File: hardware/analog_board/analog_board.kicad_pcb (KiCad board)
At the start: 4 copper layers, 125 x 90 mm, 295 parts, among them J1 2x5 牛角座, J2 Conn_02x08_Counter_Clockwise, J3 Conn_01x04_Pin, J4 Conn_01x08, J5 CH1, J6 CH1, J7 CH1, Q1 MMBT3906, Q2 MMBT3906, U1 GW2A-LV18EQ144, U11 TPS62933, U12 L7805, U13 L7905, U14 TPS7A4701xRGW, U15 TPS7A91, U19 AMS1117, U2 GD25Q32JVSS, U3 AD9747BCPZ, U4 OPA695ID, U5 OPA695ID, U6 NE5532, U8 CDCI6214RGER, Y1 ASE-10MHz

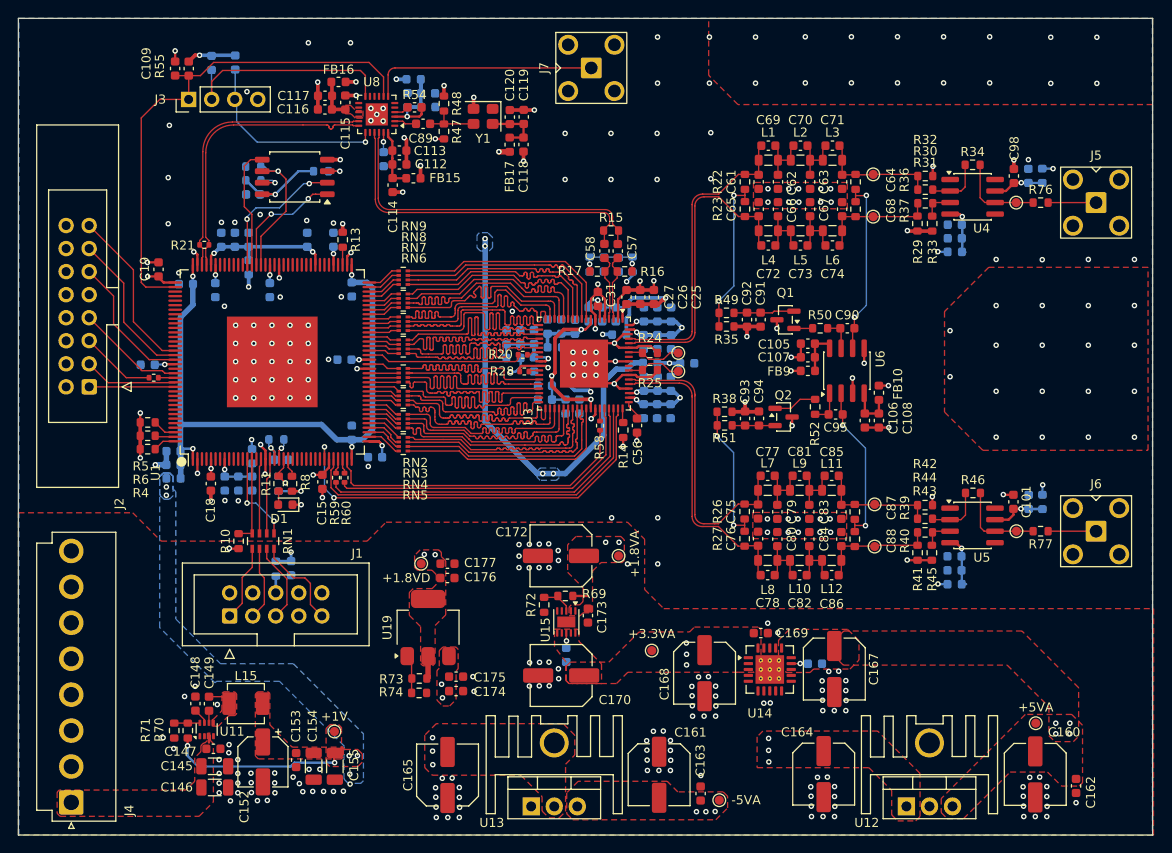
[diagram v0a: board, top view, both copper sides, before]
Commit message: debug：修正 PCB 部分错误
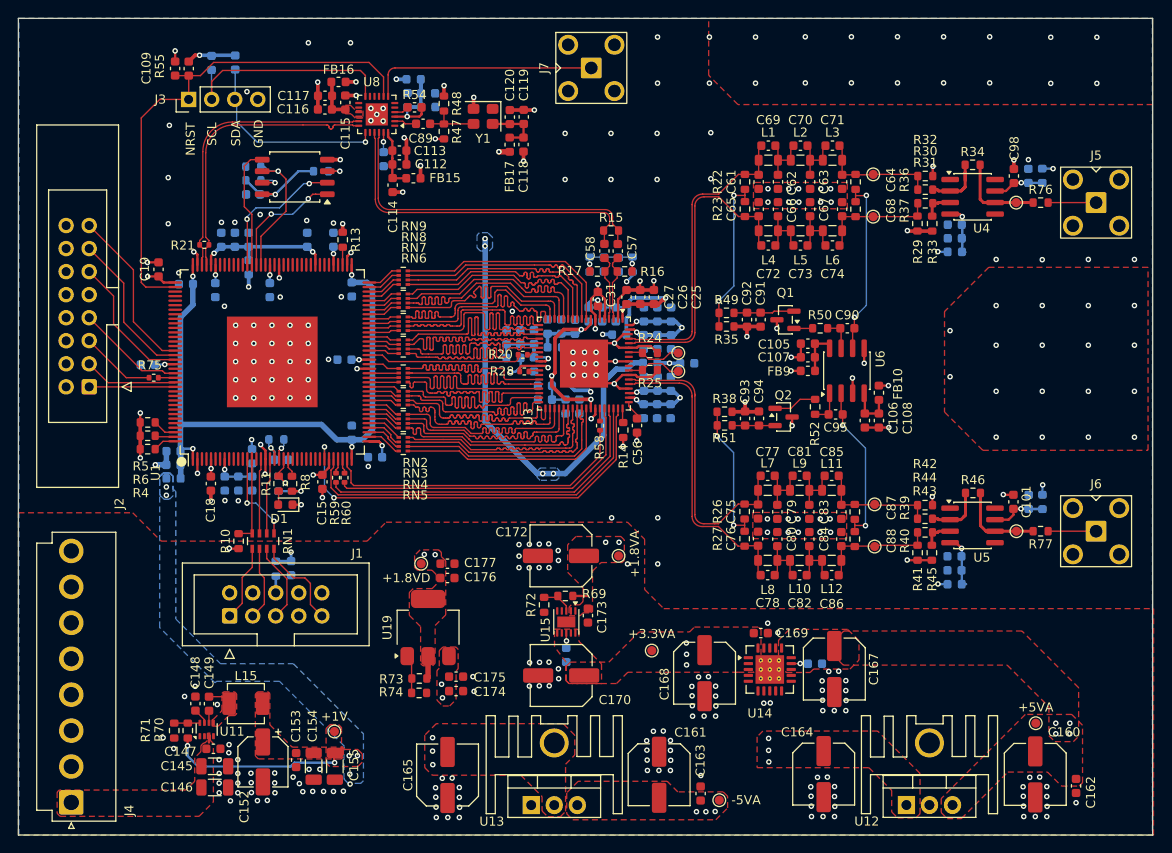
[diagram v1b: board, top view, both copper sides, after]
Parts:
- moved U12 0.15 mm to (128.0, 118.3)
- moved U13 0.14 mm to (86.6, 118.3)
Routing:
- net /DAC/OUT1: track 9.70 -> 14.0 mm
- net /DAC/OUT2: track 9.78 -> 13.9 mm
- net Net-(U4--): track 6.26 -> 9.97 mm
- net Net-(U5--): track 6.32 -> 9.04 mm
- net Net-(U4-+): track 3.61 -> 4.30 mm
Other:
- board text added: "GND"
- board text added: "NRST"
- board text added: "SCL"
- board text added: "SDA"
